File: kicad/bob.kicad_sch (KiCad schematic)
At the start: 53 parts

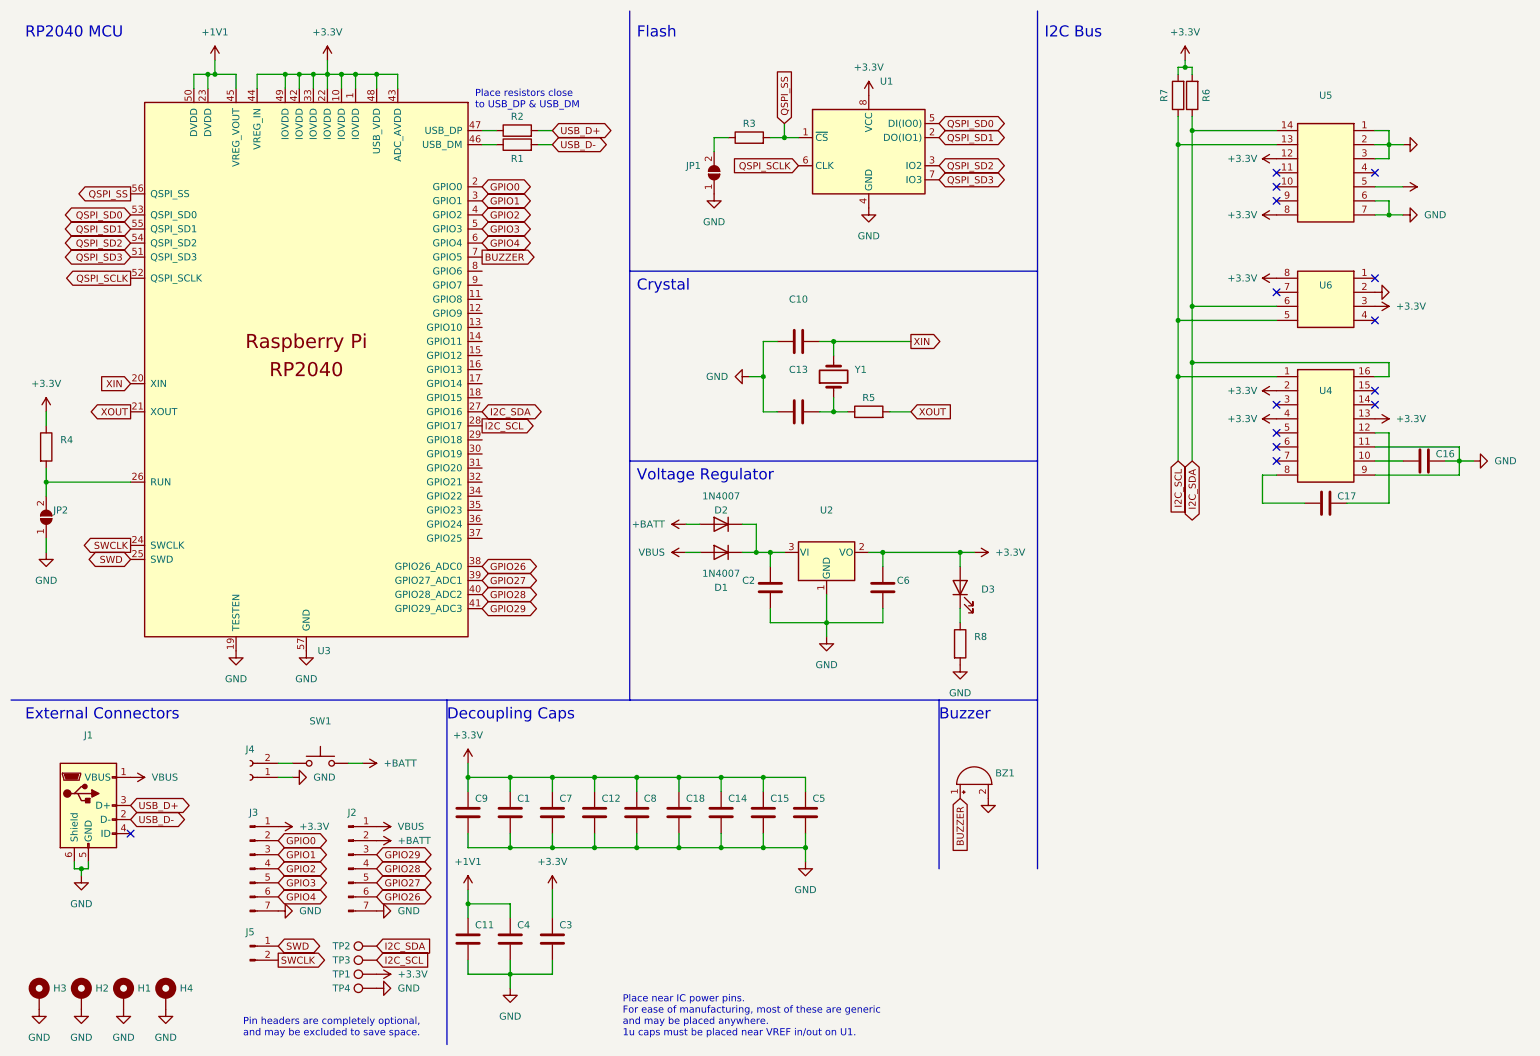
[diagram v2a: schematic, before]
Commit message: Added addresses to I2C bus
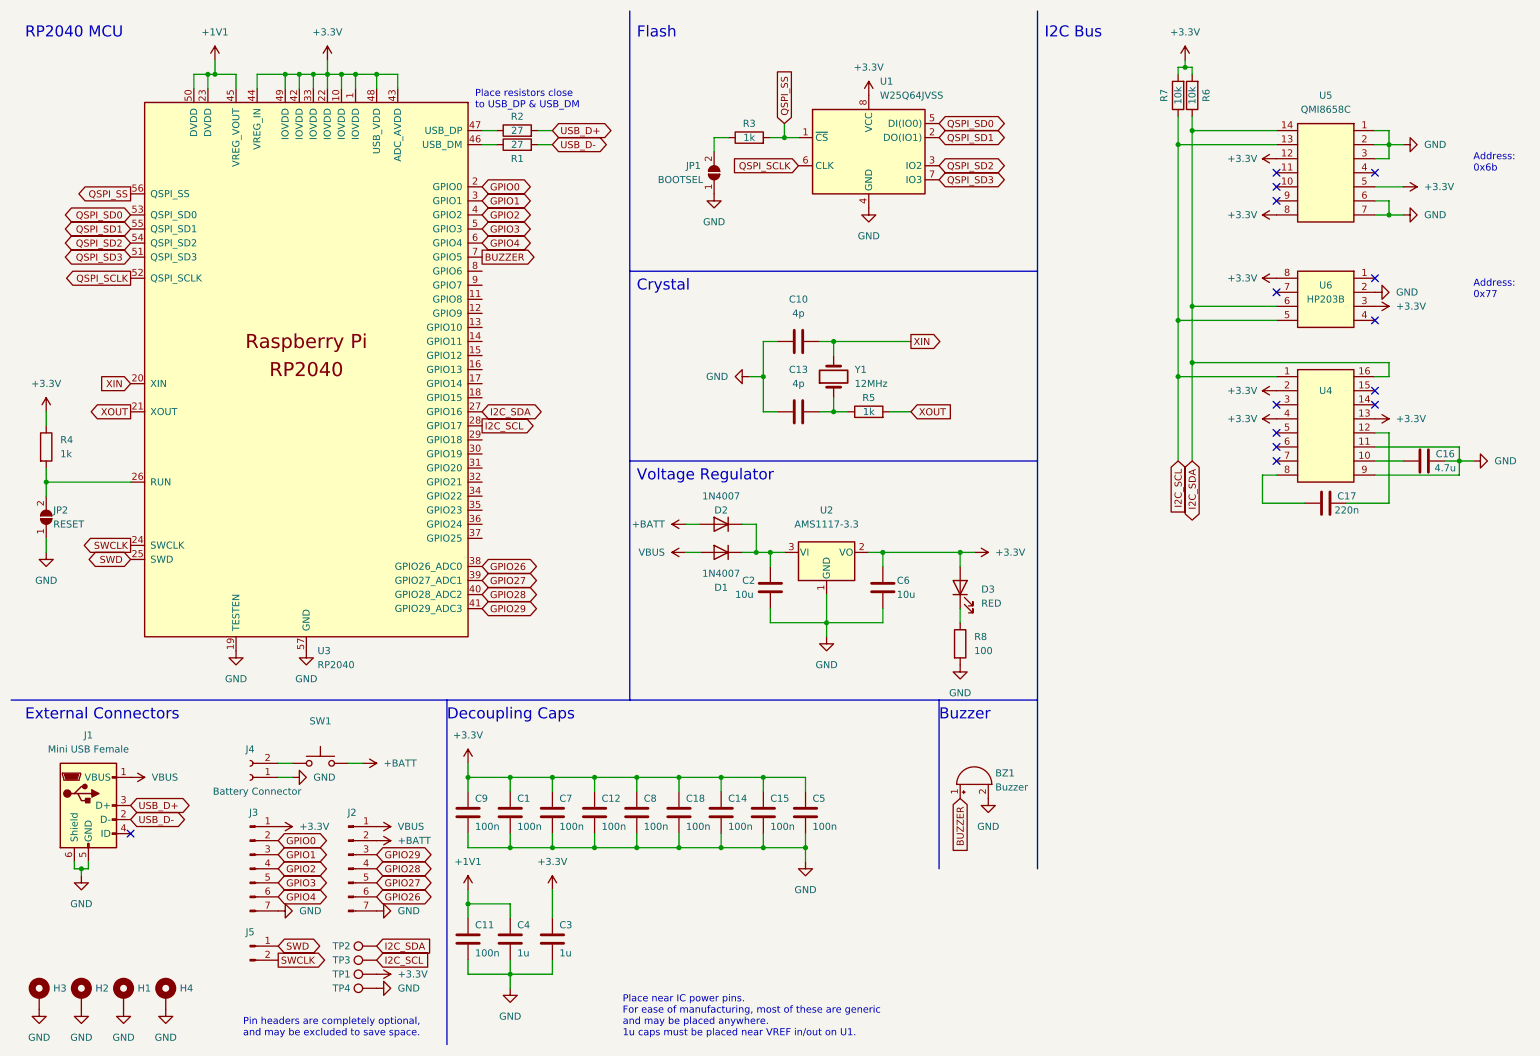
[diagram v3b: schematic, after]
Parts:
- BZ1: value (none) -> Buzzer; footprint (none) -> Buzzer_Beeper:Buzzer_12x9.5RM7.6
- C1, C11, C12, C14, C15, C18, C5, C7, C8, C9: value (none) -> 100n; footprint (none) -> Capacitor_SMD:C_0603_1608Metric
- C10, C13: value (none) -> 4p; footprint (none) -> Capacitor_SMD:C_0603_1608Metric
- C16: value (none) -> 4.7u; footprint (none) -> Capacitor_SMD:C_0603_1608Metric
- C17: value (none) -> 220n; footprint (none) -> Capacitor_SMD:C_0603_1608Metric
- C2, C6: value (none) -> 10u; footprint (none) -> Capacitor_SMD:C_0603_1608Metric
- C3, C4: value (none) -> 1u; footprint (none) -> Capacitor_SMD:C_0603_1608Metric
- D1, D2: footprint (none) -> Diode_SMD:D_SOD-123
- D3: value (none) -> RED; footprint (none) -> LED_THT:LED_D3.0mm
- H1, H2, H3, H4: value (none) -> MountingHole_Pad; footprint (none) -> MountingHole:MountingHole_2.2mm_M2_DIN965_Pad
- J1: value (none) -> Mini USB Female; footprint (none) -> Connector_USB:USB_Mini-B_Lumberg_2486_01_Horizontal
- J2, J3: value (none) -> GPIO (Optional); footprint (none) -> Connector_PinHeader_2.54mm:PinHeader_1x07_P2.54mm_Vertical_NoSilk
- J4: value (none) -> Battery Connector; footprint (none) -> Connector_Wire:Compact_Relief
- J5: value (none) -> Conn_01x03_Male; footprint (none) -> Connector_PinHeader_2.54mm:PinHeader_1x02_P2.54mm_Vertical
- JP1: value (none) -> BOOTSEL; footprint (none) -> Jumper:SolderJumper-2_P1.3mm_Open_RoundedPad1.0x1.5mm
- JP2: value (none) -> RESET; footprint (none) -> Jumper:SolderJumper-2_P1.3mm_Open_RoundedPad1.0x1.5mm
- R1, R2: value (none) -> 27; footprint (none) -> Resistor_SMD:R_0603_1608Metric_Pad0.98x0.95mm_HandSolder
- R3, R4, R5: value (none) -> 1k; footprint (none) -> Resistor_SMD:R_0603_1608Metric
- R6, R7: value (none) -> 10k; footprint (none) -> Resistor_SMD:R_0603_1608Metric
- R8: value (none) -> 100; footprint (none) -> Resistor_SMD:R_0603_1608Metric
- SW1: value (none) -> Screw Switch; footprint (none) -> Connector:Screw_Switch_M2
- TP1, TP2, TP3, TP4: value (none) -> TestPoint; footprint (none) -> TestPoint:TestPoint_Pad_D1.0mm
- U1: value (none) -> W25Q64JVSS; footprint (none) -> Package_SO:SOIC-8_5.23x5.23mm_P1.27mm
- U2: value (none) -> AMS1117-3.3; footprint (none) -> Package_TO_SOT_SMD:SOT-223-3_TabPin2
- U3: value (none) -> RP2040; footprint (none) -> RP2040_minimal:RP2040-QFN-56_HS
- U4: footprint (none) -> Silicon-Custom:LGA-16-3X3
- U5: value (none) -> QMI8658C; footprint (none) -> Silicon-Custom:14LGA_2.5x3.0
- U6: value (none) -> HP203B; footprint (none) -> RP2040_minimal:LGA-8_3.6x3.8x0.9P
- Y1: value (none) -> 12MHz; footprint (none) -> Crystal:Crystal_SMD_5032-2Pin_5.0x3.2mm
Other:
- note added: "Address: 0x6b"
- note added: "Address: 0x77"

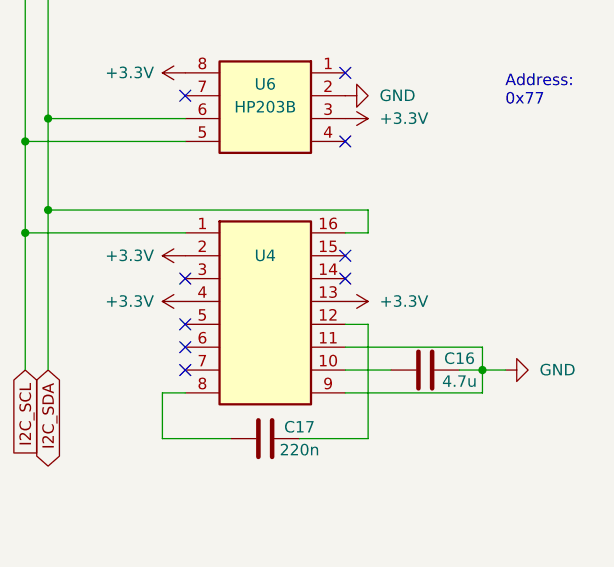
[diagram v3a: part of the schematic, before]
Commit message: Added address for QMC5883L
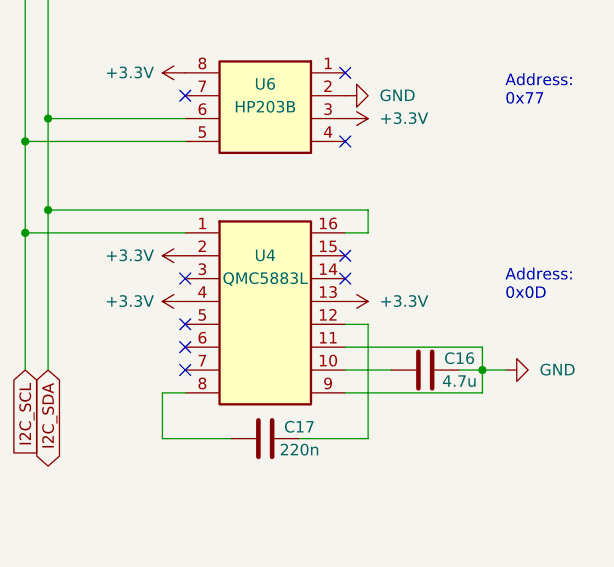
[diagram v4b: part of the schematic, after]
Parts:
- U4: value (none) -> QMC5883L
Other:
- note added: "Address: 0x0D"
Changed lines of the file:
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@@
+    (effects (font (size 1.27 1.27)) (justify left bottom))
+  )
+  (text "Address:\n0x0D" (at 274.32 85.09 0)
     (effects (font (size 1.27 1.27)) (justify left bottom))
   )
@@
     (in_bom yes) (on_board yes)
     (property "Reference" "U4" (id 0) (at 247.65 80.01 0))
-    (property "Value" "" (id 1) (at 247.65 82.55 0))
+    (property "Value" "QMC5883L" (id 1) (at 247.65 82.55 0))
     (property "Footprint" "Silicon-Custom:LGA-16-3X3" (id 2) (at 247.65 85.09 0)
       (effects (font (size 1.27 1.27)) hide)

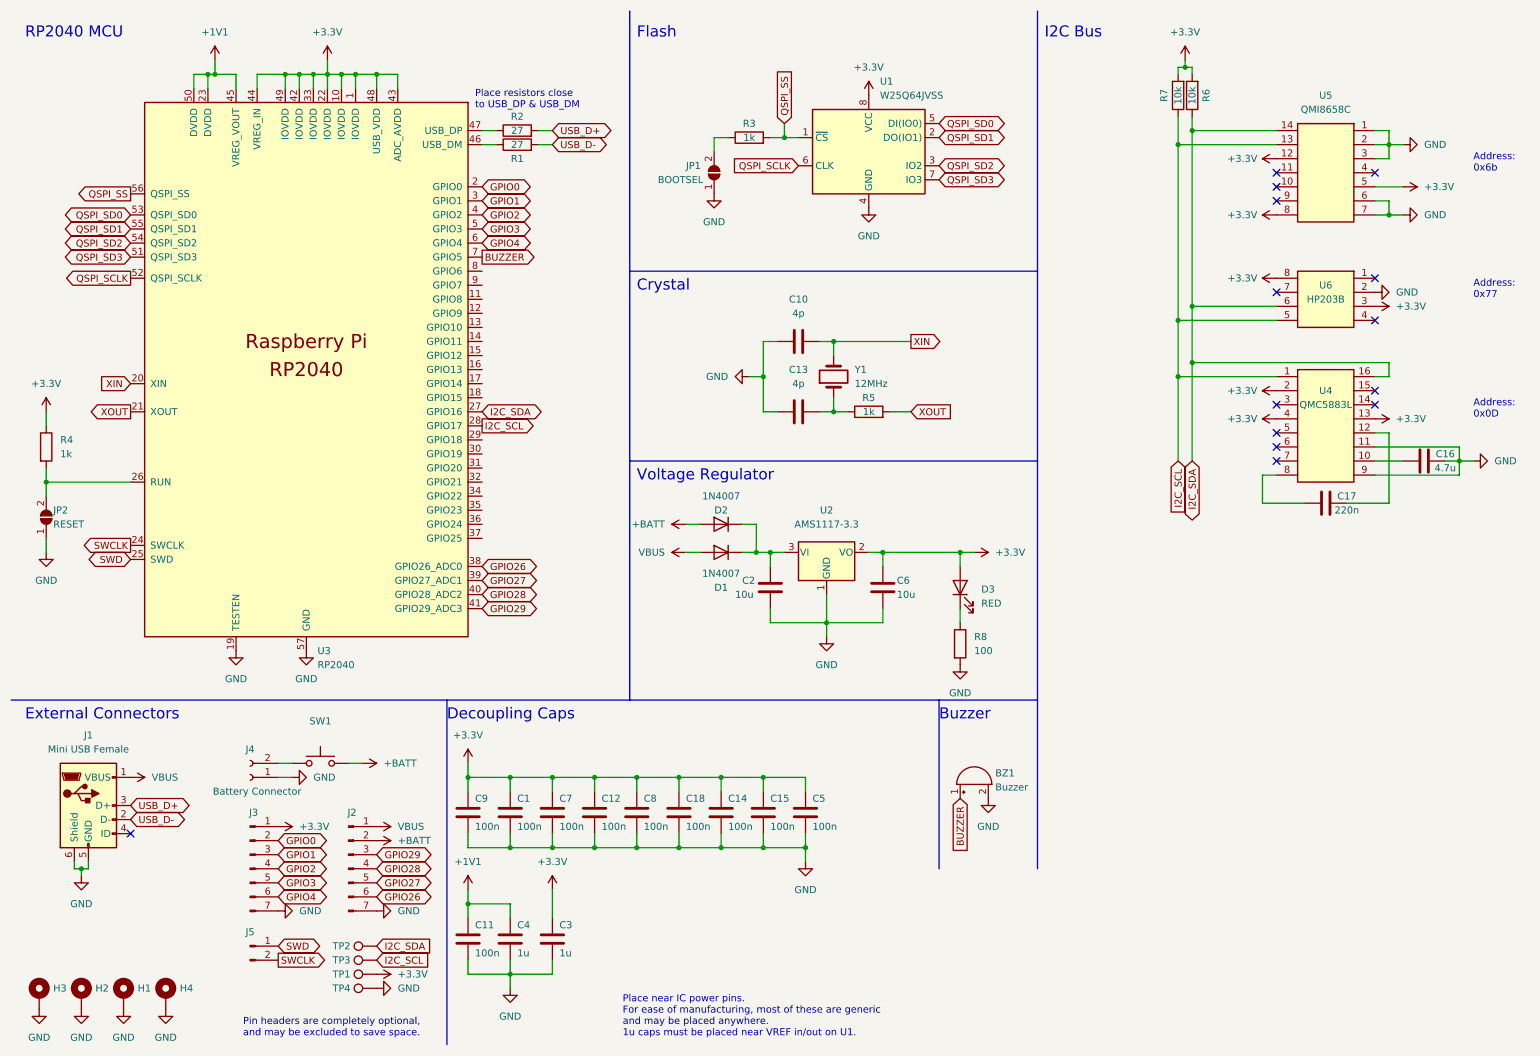
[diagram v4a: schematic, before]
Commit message: Added nice symbols to schematic
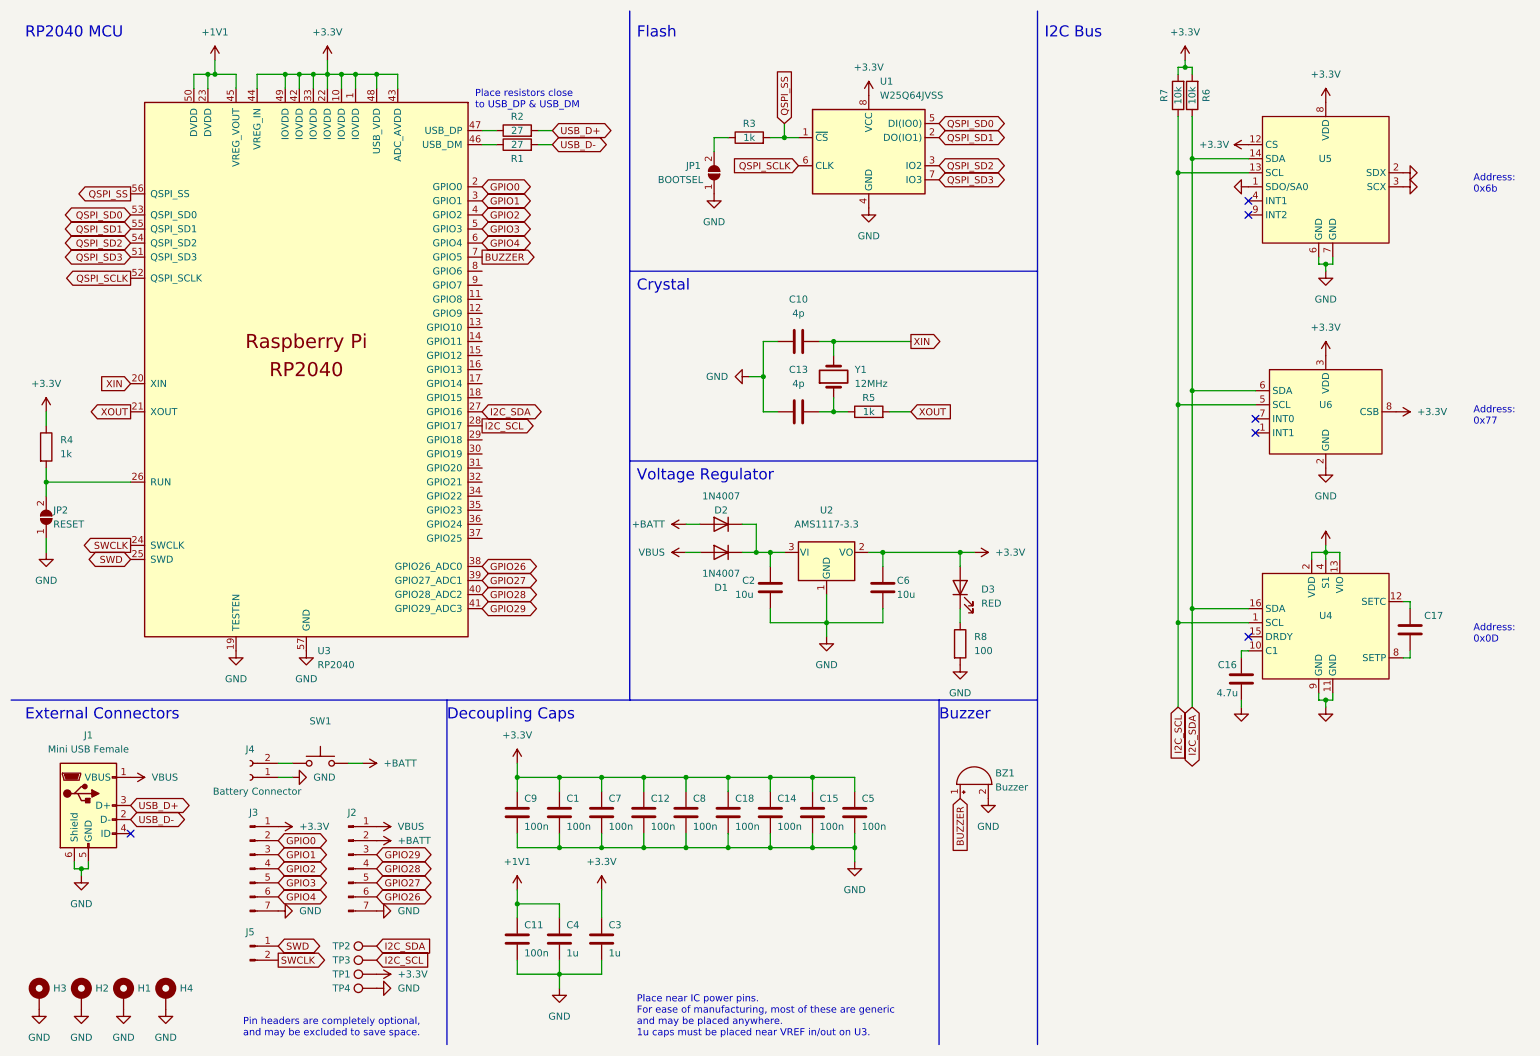
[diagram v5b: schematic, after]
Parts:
- C17: value 220n -> (none)
- U4: value QMC5883L -> (none); footprint Silicon-Custom:LGA-16-3X3 -> (none); symbol IC_Generic:IC16 -> YAR_Sensors:QMC5883L
- U5: value QMI8658C -> (none); footprint Silicon-Custom:14LGA_2.5x3.0 -> (none); symbol IC_Generic:IC14 -> YAR_Sensors:QMI8658C
- U6: value HP203B -> (none); footprint RP2040_minimal:LGA-8_3.6x3.8x0.9P -> (none); symbol IC_Generic:IC8 -> YAR_Sensors:HP203B
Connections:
- net +3V3: no longer U5.5
- net GND: now also C16.1; no longer C16.2
- net at U4.10 (C1): now also C16.2; no longer C16.1
- no-connect marks 14 -> 6
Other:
- note added: "Place near IC power pins. For ease of manufacturing, most of these are generic and may be placed anywhere. 1u caps must be placed near VREF in/out on U3."
- note removed: "Place near IC power pins. For ease of manufacturing, most of these are generic and may be placed anywhere. 1u caps must be placed near VREF in/out on U1."
- moved on the sheet: C1, C11, C12, C14, C15, C16, C17, C18, C3, C4, C5, C7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
